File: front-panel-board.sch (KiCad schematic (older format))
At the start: 26 parts

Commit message: First revision of the front panel board
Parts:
- removed CONN?: MICRO_USB, symbol cvra:MICRO_USB
- removed CONN?: SWD_DEBUG, MODULE, symbol cvra:SWD_DEBUG
- removed CONN? (x2): CAN, MODULE, symbol cvra:CAN
- removed J?: Conn_01x04, symbol Connector_Generic:Conn_01x04
- removed J?: Conn_01x11, symbol Connector_Generic:Conn_01x11
- removed J?: Conn_01x07, symbol Connector_Generic:Conn_01x07
- added D7: CRGB1318FSE, _led_rgb:CRGB1318FSE-TM, symbol led_rgb:CRGB1318FSE
- added H1, H2: M2, MountingHole:MountingHole_2.2mm_M2_ISO14580, symbol Mechanical:MountingHole
- added J1: Conn_01x05, Connector_Molex:Molex_PicoBlade_53261-0571_1x05-1MP_P1.25mm_Horizontal, symbol Connector_Generic:Conn_01x05
- added J11, J5: 0532610471, Connector_Molex:Molex_PicoBlade_53261-0471_1x04-1MP_P1.25mm_Horizontal, symbol Connector_Generic:Conn_01x04
- added J2: 10118193-0001LF, _connectors:_Micro-USB-AB-receptacle-SMT-th-no-slot, symbol cvracon:10118193-0001LF
- added J3: 0532610771, Connector_Molex:Molex_PicoBlade_53261-0771_1x07-1MP_P1.25mm_Horizontal, symbol Connector_Generic:Conn_01x07
- added J4: 0878330821, _connectors:0878330821_02x03_pin_header, symbol Connector_Generic:Conn_02x04_Odd_Even
- added J6: 0530480410, _connectors:Molex-PicoBlade-4-Edge, symbol Connector_Generic:Conn_01x04
- added J8: 0532611471, Connector_Molex:Molex_PicoBlade_53261-1471_1x14-1MP_P1.25mm_Horizontal, symbol Connector_Generic:Conn_01x14
- added R7: 130R, Resistor_SMD:R_0603_1608Metric_Pad1.05x0.95mm_HandSolder, symbol Device:R
- added R8, R9: 30R, Resistor_SMD:R_0603_1608Metric_Pad1.05x0.95mm_HandSolder, symbol Device:R
- D1: renamed from D?; footprint LED_SMD:LED_0805_2012Metric_Pad1.15x1.40mm_HandSolder -> LED_SMD:LED_0603_1608Metric_Pad1.05x0.95mm_HandSolder
- D2: renamed from D?; footprint (none) -> LED_SMD:LED_0603_1608Metric_Pad1.05x0.95mm_HandSolder
- J10: renamed from J?; value RJ45 -> 615108150221R; footprint (none) -> _connectors:615108150221R_Ethernet_MiddleMount; digikey# (none) -> 732-13727-1-ND
- J7: renamed from J?; footprint (none) -> Connector_Molex:Molex_PicoBlade_53261-0371_1x03-1MP_P1.25mm_Horizontal
- J9: renamed from J?; value Conn_01x08 -> 0532617008; footprint (none) -> Connector_Molex:Molex_PicoBlade_53261-0871_1x08-1MP_P1.25mm_Horizontal; digikey# (none) -> WM26501CT-ND
- R1, R2, R3, R4, R5, R6: renamed from R?; footprint (none) -> Resistor_SMD:R_0603_1608Metric_Pad1.05x0.95mm_HandSolder
- SW1, SW2: renamed from SW?; footprint (none) -> _switches:CFPA-1FB4-A2T
- gave numbers to parts that had none: 6
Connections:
- net labels added: DEBUG_GND, DEBUG_NRST, DEBUG_RX, DEBUG_SWCLK, DEBUG_SWDIO, DEBUG_TX, DEBUG_VCC, LED_TEAM_B, LED_TEAM_G, LED_TEAM_R, RX+, RX-, TX+, TX-, USB_D+, USB_D-, VBUS
- wire segments 81 -> 119
- no-connect marks 2 -> 3
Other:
- note added: "5 pin to avoid having\nsame connector as CAN"
- note added: "CAN Bus (Debug)"
- note added: "TODO: Vérifier pinout et sens des diodes"
- note added: "through-hole, front plate side"
- note removed: "Picoblade 4 pin\n"
- note removed: "TODO: Check if 5V is ok for our hall sensor"
- moved on the sheet: BC1, BC2, J10, J7

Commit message: Fixes after PCB review
* Bump trace width to 0.3 mm everywhere (except RJ45 conn)
* Bump clearance to 0.2 mm everywhere (except RJ45 conn)
* Reduced thermal relief width
* Improved ground plane
* Cleaned up USB connector routing / silkscreen
* Moved mechanical elements after review by mechanical engineering.
* Fixed connector labeling
* Bigger traces on CAN connectors for daisy chain

Fixes #1
Fixes #2
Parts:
- D1, D2, D3, D4, D5, D6: footprint LED_SMD:LED_0603_1608Metric_Pad1.05x0.95mm_HandSolder -> _LED_SMD:LED_0603_RightAngle
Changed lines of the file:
@@
 F 0 "D1" H 9393 845 50  0000 C CNN
 F 1 "LED_GREEN" H 9393 936 50  0000 C CNN
-F 2 "LED_SMD:LED_0603_1608Metric_Pad1.05x0.95mm_HandSolder" H 9400 1100 50  0001 C CNN
+F 2 "_LED_SMD:LED_0603_RightAngle" H 9400 1100 50  0001 C CNN
 F 3 "https://media.digikey.com/pdf/Data%20Sheets/Lite-On%20PDFs/LTST-S270GKT.pdf" H 9400 1100 50  0001 C CNN
 F 4 "160-1475-1-ND" H 9400 1100 50  0001 C CNN "digikey#"
@@
 F 0 "D2" H 9393 1345 50  0000 C CNN
 F 1 "LED_BLUE" H 9393 1436 50  0000 C CNN
-F 2 "LED_SMD:LED_0603_1608Metric_Pad1.05x0.95mm_HandSolder" H 9400 1600 50  0001 C CNN
-F 3 "~" H 9400 1600 50  0001 C CNN
+F 2 "_LED_SMD:LED_0603_RightAngle" H 9400 1600 50  0001 C CNN
+F 3 "http://www.inolux-corp.com/datasheet/SMDLED/Mono%20Color%20Side%20View/IN-S63AS%20Series_V1.0.pdf" H 9400 1600 50  0001 C CNN
 F 4 "1830-1029-1-ND" H 9400 1600 50  0001 C CNN "digikey#"
 	1    9400 1600
@@
 F 0 "D3" H 9393 1845 50  0000 C CNN
 F 1 "LED_RED" H 9393 1936 50  0000 C CNN
-F 2 "LED_SMD:LED_0603_1608Metric_Pad1.05x0.95mm_HandSolder" H 9400 2100 50  0001 C CNN
+F 2 "_LED_SMD:LED_0603_RightAngle" H 9400 2100 50  0001 C CNN
 F 3 "http://optoelectronics.liteon.com/upload/download/DS22-2000-210/LTST-S270KRKT.pdf" H 9400 2100 50  0001 C CNN
 F 4 "160-1479-1-ND" H 9400 2100 50  0001 C CNN "digikey#"
@@
 F 0 "D4" H 9393 2295 50  0000 C CNN
 F 1 "LED_ORANGE" H 9393 2386 50  0000 C CNN
-F 2 "LED_SMD:LED_0603_1608Metric_Pad1.05x0.95mm_HandSolder" H 9400 2550 50  0001 C CNN
+F 2 "_LED_SMD:LED_0603_RightAngle" H 9400 2550 50  0001 C CNN
 F 3 "http://optoelectronics.liteon.com/upload/download/DS22-2000-209/LTST-S270KFKT.pdf" H 9400 2550 50  0001 C CNN
 F 4 "160-1477-1-ND" H 9400 2550 50  0001 C CNN "digikey#"
@@
 F 0 "D5" H 9393 2745 50  0000 C CNN
 F 1 "LED_ORANGE" H 9393 2836 50  0000 C CNN
-F 2 "LED_SMD:LED_0603_1608Metric_Pad1.05x0.95mm_HandSolder" H 9400 3000 50  0001 C CNN
+F 2 "_LED_SMD:LED_0603_RightAngle" H 9400 3000 50  0001 C CNN
 F 3 "http://optoelectronics.liteon.com/upload/download/DS22-2000-209/LTST-S270KFKT.pdf" H 9400 3000 50  0001 C CNN
 F 4 "160-1477-1-ND" H 9400 3000 50  0001 C CNN "digikey#"
@@
 F 0 "D6" H 9393 3245 50  0000 C CNN
 F 1 "LED_ORANGE" H 9393 3336 50  0000 C CNN
-F 2 "LED_SMD:LED_0603_1608Metric_Pad1.05x0.95mm_HandSolder" H 9400 3500 50  0001 C CNN
+F 2 "_LED_SMD:LED_0603_RightAngle" H 9400 3500 50  0001 C CNN
 F 3 "http://optoelectronics.liteon.com/upload/download/DS22-2000-209/LTST-S270KFKT.pdf" H 9400 3500 50  0001 C CNN
 F 4 "160-1477-1-ND" H 9400 3500 50  0001 C CNN "digikey#"

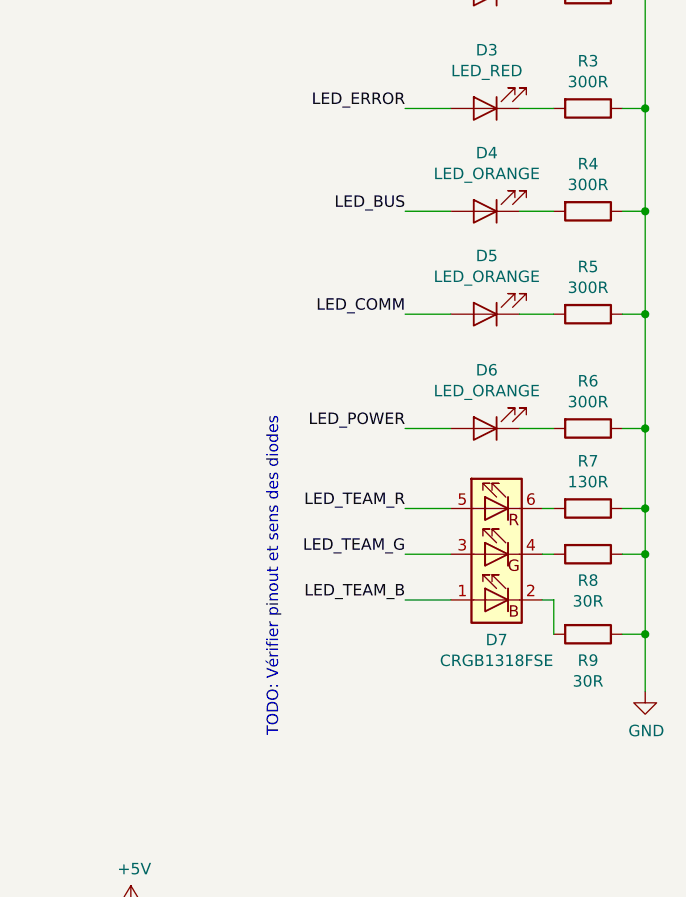
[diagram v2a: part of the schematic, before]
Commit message: Use red LEDs instead of orange ones, as they are OoS
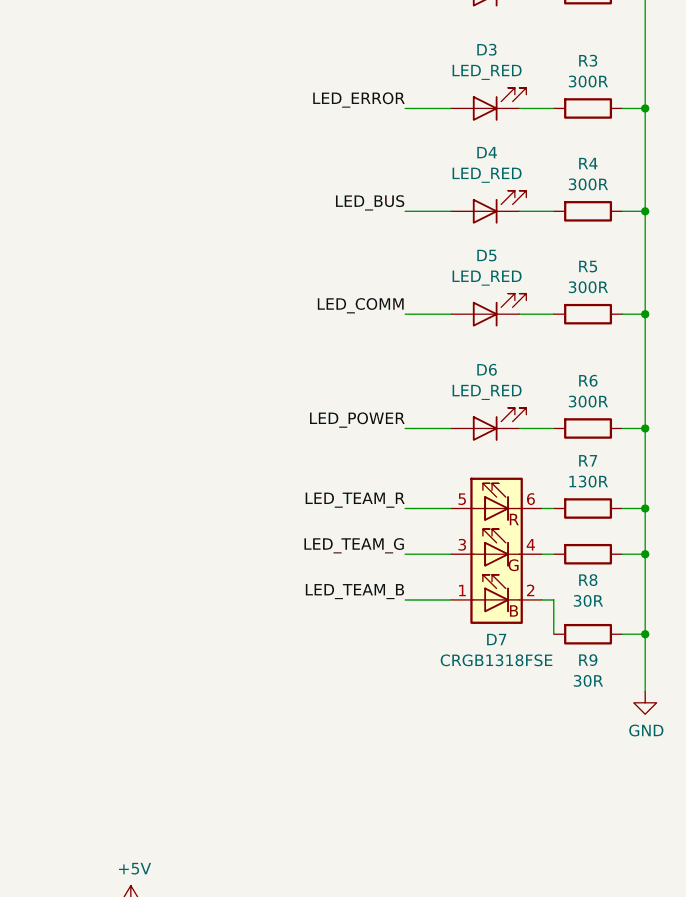
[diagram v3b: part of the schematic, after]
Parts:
- D4, D5, D6: value LED_ORANGE -> LED_RED; digikey# 160-1477-1-ND -> (none)
- H1, H2: DNP (none) -> 1
- J1: digikey# (none) -> WM7623CT-ND
- J7: digikey# (none) -> WM7621CT-ND
- R1: digikey# (none) -> 311-56.0HRCT-ND
- R3: digikey# (none) -> 311-300HRCT-ND
- R7: digikey# (none) -> 311-130HRCT-ND
- R8: digikey# (none) -> 311-30.0HRCT-ND
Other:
- note removed: "TODO: Vérifier pinout et sens des diodes"
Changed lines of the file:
@@
 F 2 "Resistor_SMD:R_0603_1608Metric_Pad1.05x0.95mm_HandSolder" V 9780 1100 50  0001 C CNN
 F 3 "~" H 9850 1100 50  0001 C CNN
+F 4 "311-56.0HRCT-ND" V 9850 1100 50  0001 C CNN "digikey#"
 	1    9850 1100
 	0    1    1    0
@@
 P 9400 2550
 F 0 "D4" H 9393 2295 50  0000 C CNN
-F 1 "LED_ORANGE" H 9393 2386 50  0000 C CNN
+F 1 "LED_RED" H 9393 2386 50  0000 C CNN
 F 2 "_LED_SMD:LED_0603_RightAngle" H 9400 2550 50  0001 C CNN
 F 3 "http://optoelectronics.liteon.com/upload/download/DS22-2000-209/LTST-S270KFKT.pdf" H 9400 2550 50  0001 C CNN
-F 4 "160-1477-1-ND" H 9400 2550 50  0001 C CNN "digikey#"
 	1    9400 2550
 	-1   0    0    1
@@
 F 2 "Resistor_SMD:R_0603_1608Metric_Pad1.05x0.95mm_HandSolder" V 9780 2100 50  0001 C CNN
 F 3 "~" H 9850 2100 50  0001 C CNN
+F 4 "311-300HRCT-ND" V 9850 2100 50  0001 C CNN "digikey#"
 	1    9850 2100
 	0    1    1    0
@@
 P 9400 3000
 F 0 "D5" H 9393 2745 50  0000 C CNN
-F 1 "LED_ORANGE" H 9393 2836 50  0000 C CNN
+F 1 "LED_RED" H 9393 2836 50  0000 C CNN
 F 2 "_LED_SMD:LED_0603_RightAngle" H 9400 3000 50  0001 C CNN
 F 3 "http://optoelectronics.liteon.com/upload/download/DS22-2000-209/LTST-S270KFKT.pdf" H 9400 3000 50  0001 C CNN
-F 4 "160-1477-1-ND" H 9400 3000 50  0001 C CNN "digikey#"
 	1    9400 3000
 	-1   0    0    1
@@
 F 2 "Connector_Molex:Molex_PicoBlade_53261-0371_1x03-1MP_P1.25mm_Horizontal" H 8100 5750 50  0001 C CNN
 F 3 "~" H 8100 5750 50  0001 C CNN
+F 4 "WM7621CT-ND" H 8100 5750 50  0001 C CNN "digikey#"
 	1    8100 5750
 	1    0    0    -1
@@
 F 2 "MountingHole:MountingHole_2.2mm_M2_ISO14580" H 5800 6850 50  0001 C CNN
 F 3 "~" H 5800 6850 50  0001 C CNN
+F 4 "1" H 5800 6850 50  0001 C CNN "DNP"
 	1    5800 6850
 	1    0    0    -1
@@
 F 2 "MountingHole:MountingHole_2.2mm_M2_ISO14580" H 5800 7100 50  0001 C CNN
 F 3 "~" H 5800 7100 50  0001 C CNN
+F 4 "1" H 5800 7100 50  0001 C CNN "DNP"
 	1    5800 7100
 	1    0    0    -1
@@
 F 2 "Resistor_SMD:R_0603_1608Metric_Pad1.05x0.95mm_HandSolder" V 9780 3850 50  0001 C CNN
 F 3 "~" H 9850 3850 50  0001 C CNN
+F 4 "311-130HRCT-ND" V 9850 3850 50  0001 C CNN "digikey#"
 	1    9850 3850
 	0    1    1    0
@@
 F 2 "Resistor_SMD:R_0603_1608Metric_Pad1.05x0.95mm_HandSolder" V 9780 4050 50  0001 C CNN
 F 3 "~" H 9850 4050 50  0001 C CNN
+F 4 "311-30.0HRCT-ND" V 9850 4050 50  0001 C CNN "digikey#"
 	1    9850 4050
 	0    1    1    0
@@
 P 9400 3500
 F 0 "D6" H 9393 3245 50  0000 C CNN
-F 1 "LED_ORANGE" H 9393 3336 50  0000 C CNN
+F 1 "LED_RED" H 9393 3336 50  0000 C CNN
 F 2 "_LED_SMD:LED_0603_RightAngle" H 9400 3500 50  0001 C CNN
 F 3 "http://optoelectronics.liteon.com/upload/download/DS22-2000-209/LTST-S270KFKT.pdf" H 9400 3500 50  0001 C CNN
-F 4 "160-1477-1-ND" H 9400 3500 50  0001 C CNN "digikey#"
 	1    9400 3500
 	-1   0    0    1
 $EndComp
-Text Notes 8500 4850 1    50   ~ 0
-TODO: Vérifier pinout et sens des diodes
 $Comp
 L Connector_Generic:Conn_01x04 J11
@@
 F 2 "Connector_Molex:Molex_PicoBlade_53261-0571_1x05-1MP_P1.25mm_Horizontal" H 1100 1150 50  0001 C CNN
 F 3 "~" H 1100 1150 50  0001 C CNN
+F 4 "WM7623CT-ND" H 1100 1150 50  0001 C CNN "digikey#"
 	1    1100 1150
 	-1   0    0    -1

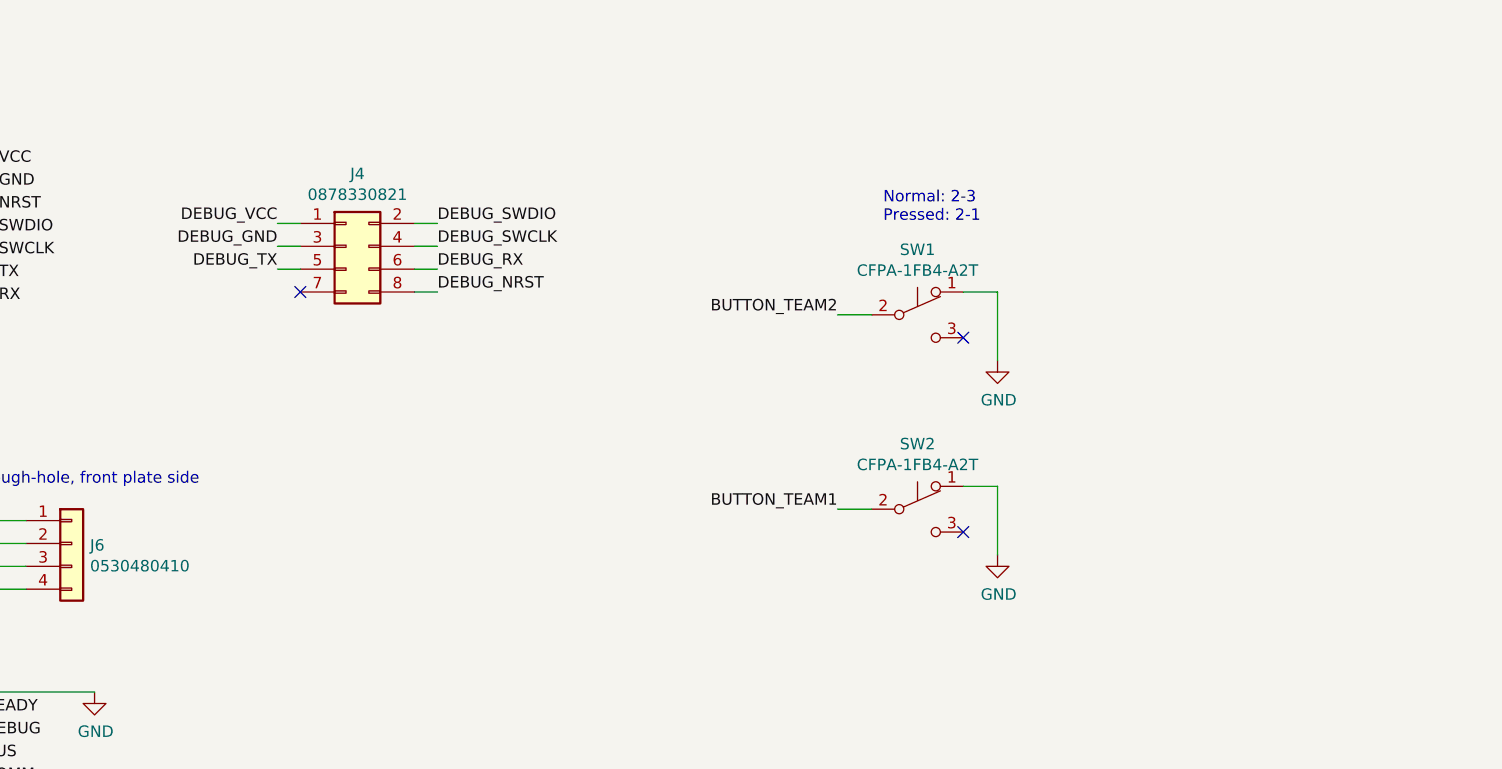
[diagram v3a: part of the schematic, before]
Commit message: Add notes on female programming cable manufacturing
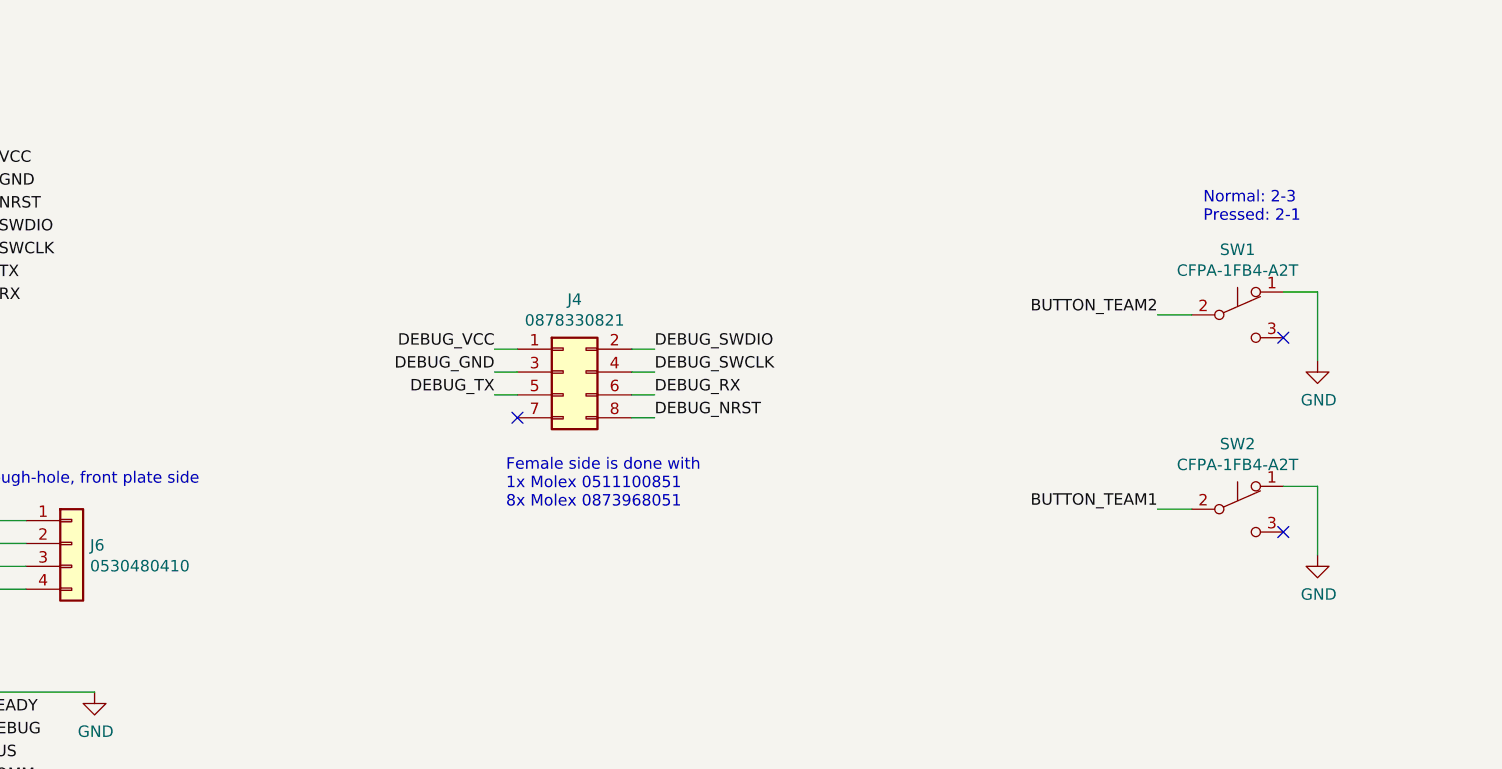
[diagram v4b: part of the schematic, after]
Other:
- note added: "Female side is done with\n1x Molex 0511100851\n8x Molex 0873968051"
- moved on the sheet: J4, SW1, SW2
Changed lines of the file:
@@
 L Switch:SW_Push_SPDT SW1
 U 1 1 5E7575A2
-P 5700 3100
-F 0 "SW1" H 5700 3385 50  0000 C CNN
-F 1 "CFPA-1FB4-A2T" H 5700 3294 50  0000 C CNN
-F 2 "_switches:CFPA-1FB4-A2T" H 5700 3100 50  0001 C CNN
-F 3 "https://www.nidec-copal-electronics.com/e/catalog/switch/cfpa.pdf" H 5700 3100 50  0001 C CNN
-F 4 "563-1246-1-ND" H 5700 3100 50  0001 C CNN "digikey#"
-F 5 "" H 5700 3100 50  0001 C CNN "Field5"
-	1    5700 3100
+P 7100 3100
+F 0 "SW1" H 7100 3385 50  0000 C CNN
+F 1 "CFPA-1FB4-A2T" H 7100 3294 50  0000 C CNN
+F 2 "_switches:CFPA-1FB4-A2T" H 7100 3100 50  0001 C CNN
+F 3 "https://www.nidec-copal-electronics.com/e/catalog/switch/cfpa.pdf" H 7100 3100 50  0001 C CNN
+F 4 "563-1246-1-ND" H 7100 3100 50  0001 C CNN "digikey#"
+F 5 "" H 7100 3100 50  0001 C CNN "Field5"
+	1    7100 3100
 	1    0    0    -1
 $EndComp
@@
 	1    0    0    -1
 $EndComp
-Text Notes 5550 2700 0    50   ~ 0
+Text Notes 6950 2700 0    50   ~ 0
 Normal: 2-3\nPressed: 2-1
-Text Label 5350 3100 2    50   ~ 0
+Text Label 6750 3100 2    50   ~ 0
 BUTTON_TEAM2
 $Comp
 L power:GND #PWR05
 U 1 1 5E761EC6
-P 6050 3300
-F 0 "#PWR05" H 6050 3050 50  0001 C CNN
-F 1 "GND" H 6055 3127 50  0000 C CNN
-F 2 "" H 6050 3300 50  0001 C CNN
-F 3 "" H 6050 3300 50  0001 C CNN
-	1    6050 3300
-	1    0    0    -1
-$EndComp
-Wire Wire Line
-	5900 3000 6050 3000
-Wire Wire Line
-	6050 3000 6050 3300
-NoConn ~ 5900 3200
+P 7450 3300
+F 0 "#PWR05" H 7450 3050 50  0001 C CNN
+F 1 "GND" H 7455 3127 50  0000 C CNN
+F 2 "" H 7450 3300 50  0001 C CNN
+F 3 "" H 7450 3300 50  0001 C CNN
+	1    7450 3300
+	1    0    0    -1
+$EndComp
+Wire Wire Line
+	7300 3000 7450 3000
+Wire Wire Line
+	7450 3000 7450 3300
+NoConn ~ 7300 3200
 $Comp
 L Switch:SW_Push_SPDT SW2
 U 1 1 5E771084
-P 5700 3950
-F 0 "SW2" H 5700 4235 50  0000 C CNN
-F 1 "CFPA-1FB4-A2T" H 5700 4144 50  0000 C CNN
-F 2 "_switches:CFPA-1FB4-A2T" H 5700 3950 50  0001 C CNN
-F 3 "https://www.nidec-copal-electronics.com/e/catalog/switch/cfpa.pdf" H 5700 3950 50  0001 C CNN
-F 4 "563-1246-1-ND" H 5700 3950 50  0001 C CNN "digikey#"
-F 5 "" H 5700 3950 50  0001 C CNN "Field5"
-	1    5700 3950
+P 7100 3950
+F 0 "SW2" H 7100 4235 50  0000 C CNN
+F 1 "CFPA-1FB4-A2T" H 7100 4144 50  0000 C CNN
+F 2 "_switches:CFPA-1FB4-A2T" H 7100 3950 50  0001 C CNN
+F 3 "https://www.nidec-copal-electronics.com/e/catalog/switch/cfpa.pdf" H 7100 3950 50  0001 C CNN
+F 4 "563-1246-1-ND" H 7100 3950 50  0001 C CNN "digikey#"
+F 5 "" H 7100 3950 50  0001 C CNN "Field5"
+	1    7100 3950
 	1    0    0    -1
 $EndComp
@@
 	1    0    0    -1
 $EndComp
-Text Label 5350 3950 2    50   ~ 0
+Text Label 6750 3950 2    50   ~ 0
 BUTTON_TEAM1
 $Comp
 L power:GND #PWR07
 U 1 1 5E77109B
-P 6050 4150
-F 0 "#PWR07" H 6050 3900 50  0001 C CNN
-F 1 "GND" H 6055 3977 50  0000 C CNN
-F 2 "" H 6050 4150 50  0001 C CNN
-F 3 "" H 6050 4150 50  0001 C CNN
-	1    6050 4150
-	1    0    0    -1
-$EndComp
-Wire Wire Line
-	5900 3850 6050 3850
-Wire Wire Line
-	6050 3850 6050 4150
-NoConn ~ 5900 4050
+P 7450 4150
+F 0 "#PWR07" H 7450 3900 50  0001 C CNN
+F 1 "GND" H 7455 3977 50  0000 C CNN
+F 2 "" H 7450 4150 50  0001 C CNN
+F 3 "" H 7450 4150 50  0001 C CNN
+	1    7450 4150
+	1    0    0    -1
+$EndComp
+Wire Wire Line
+	7300 3850 7450 3850
+Wire Wire Line
+	7450 3850 7450 4150
+NoConn ~ 7300 4050
 $Comp
 L Connector_Generic:Conn_01x04 J6
@@
 L Connector_Generic:Conn_02x04_Odd_Even J4
 U 1 1 5E7A15C0
-P 3200 2800
-F 0 "J4" H 3250 3117 50  0000 C CNN
-F 1 "0878330821" H 3250 3026 50  0000 C CNN
-F 2 "_connectors:0878330821_02x03_pin_header" H 3200 2800 50  0001 C CNN
-F 3 "~" H 3200 2800 50  0001 C CNN
-F 4 "WM23634-ND" H 3200 2800 50  0001 C CNN "digikey#"
-	1    3200 2800
+P 4150 3350
+F 0 "J4" H 4200 3667 50  0000 C CNN
+F 1 "0878330821" H 4200 3576 50  0000 C CNN
+F 2 "_connectors:0878330821_02x03_pin_header" H 4150 3350 50  0001 C CNN
+F 3 "~" H 4150 3350 50  0001 C CNN
+F 4 "WM23634-ND" H 4150 3350 50  0001 C CNN "digikey#"
+	1    4150 3350
 	1    0    0    -1
 $EndComp
@@
 Wire Wire Line
 	1150 3050 1400 3050
-Text Label 2900 2700 2    50   ~ 0
+Text Label 3850 3250 2    50   ~ 0
 DEBUG_VCC
-Text Label 2900 2800 2    50   ~ 0
+Text Label 3850 3350 2    50   ~ 0
 DEBUG_GND
-NoConn ~ 3000 3000
-Text Label 3600 3000 0    50   ~ 0
+NoConn ~ 3950 3550
+Text Label 4550 3550 0    50   ~ 0
 DEBUG_NRST
-Text Label 3600 2700 0    50   ~ 0
+Text Label 4550 3250 0    50   ~ 0
 DEBUG_SWDIO
-Text Label 3600 2800 0    50   ~ 0
+Text Label 4550 3350 0    50   ~ 0
 DEBUG_SWCLK
-Text Label 2900 2900 2    50   ~ 0
+Text Label 3850 3450 2    50   ~ 0
 DEBUG_TX
-Text Label 3600 2900 0    50   ~ 0
+Text Label 4550 3450 0    50   ~ 0
 DEBUG_RX
 Wire Wire Line
-	2900 2700 3000 2700
-Wire Wire Line
-	2900 2800 3000 2800
-Wire Wire Line
-	2900 2900 3000 2900
-Wire Wire Line
-	3500 2700 3600 2700
-Wire Wire Line
-	3500 2800 3600 2800
-Wire Wire Line
-	3500 2900 3600 2900
-Wire Wire Line
-	3500 3000 3600 3000
+	3850 3250 3950 3250
+Wire Wire Line
+	3850 3350 3950 3350
+Wire Wire Line
+	3850 3450 3950 3450
+Wire Wire Line
+	4450 3250 4550 3250
+Wire Wire Line
+	4450 3350 4550 3350
+Wire Wire Line
+	4450 3450 4550 3450
+Wire Wire Line
+	4450 3550 4550 3550
 $Comp
 L Mechanical:MountingHole H1
@@
 5 pin to avoid having\nsame connector as CAN
 Wire Wire Line
-	5350 3100 5500 3100
-Wire Wire Line
-	5350 3950 5500 3950
+	6750 3100 6900 3100
+Wire Wire Line
+	6750 3950 6900 3950
 Text Label 1450 5150 0    50   ~ 0
 LED_COMM
+Text Notes 3900 3950 0    50   ~ 0
+Female side is done with\n1x Molex 0511100851\n8x Molex 0873968051
 $EndSCHEMATC
